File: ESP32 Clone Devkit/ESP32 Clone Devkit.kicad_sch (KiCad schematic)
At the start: 34 parts, among them J1 USB_B_Micro, J2 Conn_01x19_Pin, J3 Conn_01x19_Pin, Q1 MMSS8050-H-TP, Q2 MMSS8050-H-TP, SW1 SW_Push, SW2 SW_Push, U1 CP2102N-A02-GQFN28, U2 AMS1117-3.3

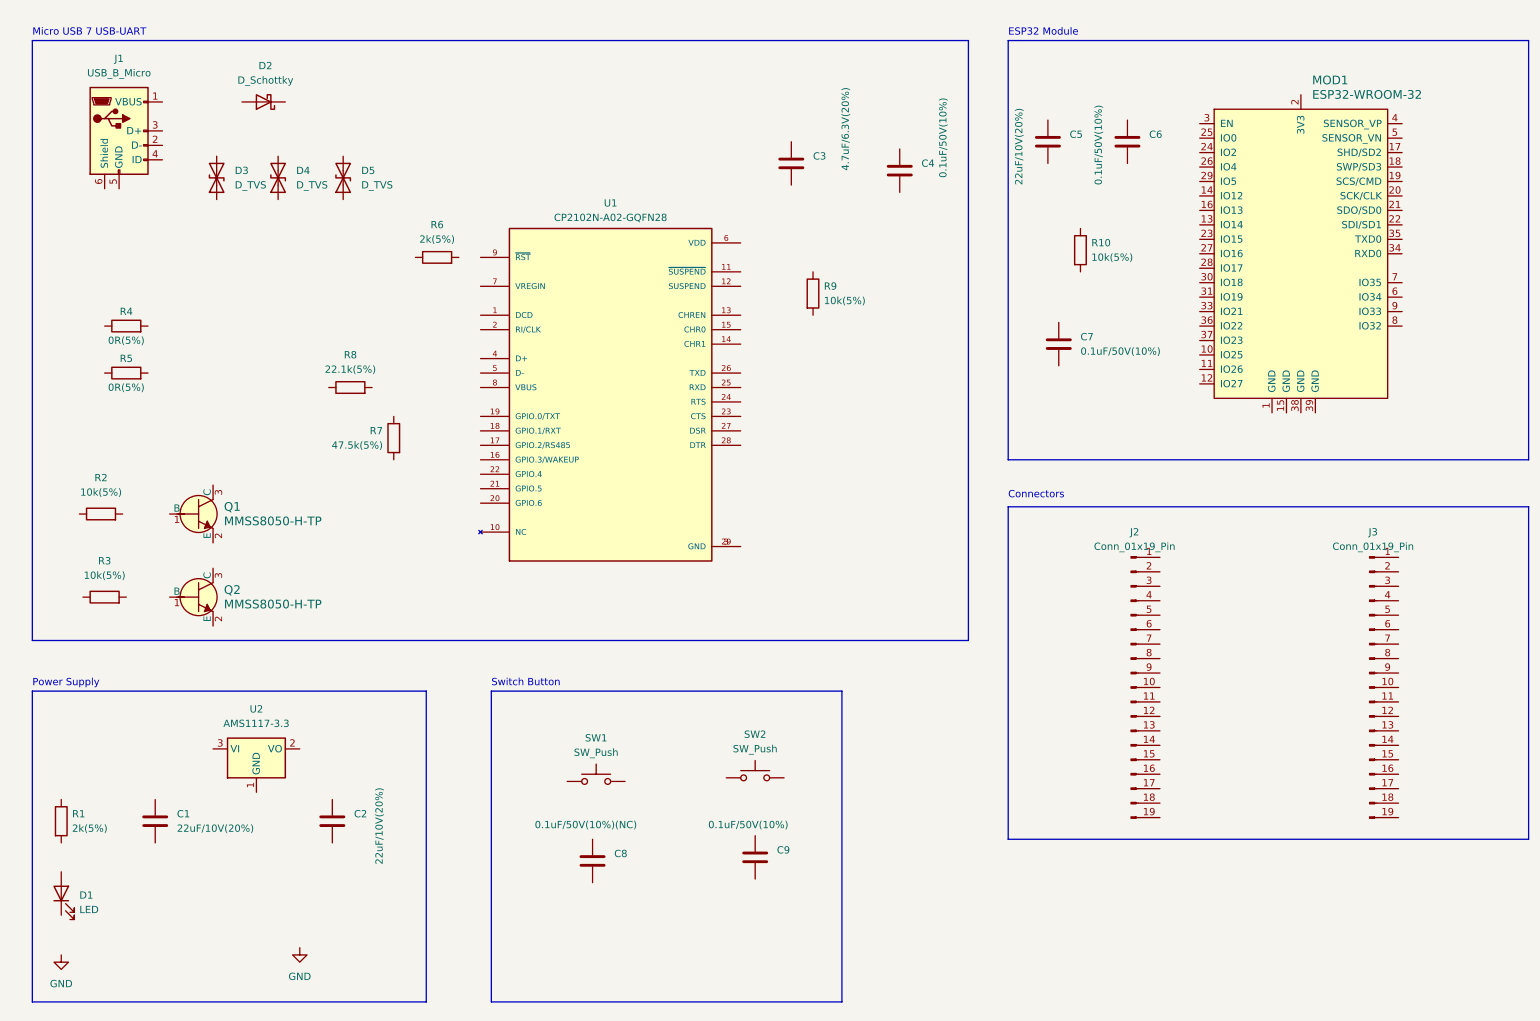
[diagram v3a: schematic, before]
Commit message: terminate wiring
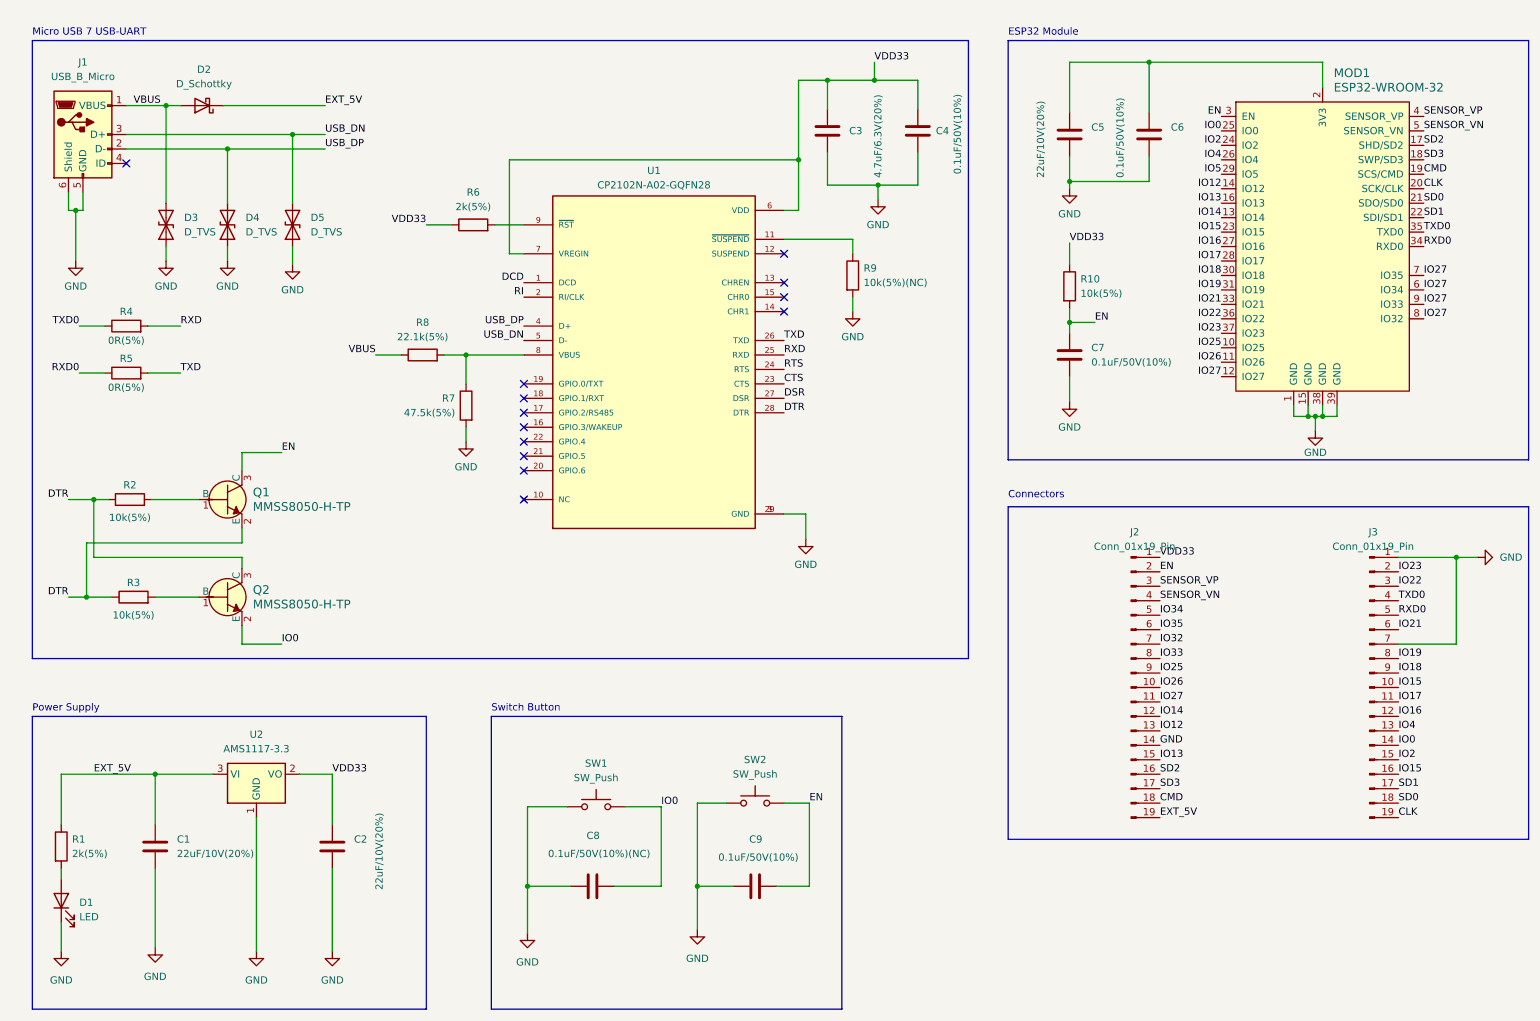
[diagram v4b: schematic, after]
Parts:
- R9: value 10k(5%) -> 10k(5%)(NC)
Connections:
- net GND: now also C1.2, C2.2, C3.2, C4.2, C5.2, C6.2, C7.2, C8.1, C9.1, D1.1 (K), D3.1 (A1), D4.1 (A1), D5.1 (A1), J1.5 (GND), J1.6 (Shield), J2.14 (Pin_14), J3.1 (Pin_1), J3.7 (Pin_7), MOD1.1 (GND), MOD1.15 (GND), MOD1.38 (GND), MOD1.39 (GND), R7.2, R9.2, SW1.1, SW2.1, U1.29 (GND), U1.3 (GND), U2.1 (GND)
- net VDD33: now reaches C3.1
- net VDD33: now also C2.1, C4.1, J2.1 (Pin_1), R10.1, R6.1, U1.6 (VDD), U1.7 (VREGIN), U2.2 (VO)
- net at Q2.1 (B): now also R3.2
- net IO0: now reaches Q2.2 (E)
- net IO0: now also C8.2, J3.14 (Pin_14), MOD1.25 (IO0), SW1.2
- net DTR: now reaches Q2.3 (C)
- net DTR: now also Q1.2 (E), R2.1, R3.1, U1.28 (DTR)
- net EXT_5V: now reaches R1.1
- net EXT_5V: now also C1.1, D2.1 (K), J2.19 (Pin_19), U2.3 (VI)
- net at R1.2: now also D1.2 (A)
- net at R6.2: now also U1.9 (~{RST})
- net at Q1.1 (B): now also R2.2
- net EN: now reaches Q1.3 (C)
- net EN: now also C7.1, C9.2, J2.2 (Pin_2), MOD1.3 (EN), R10.2, SW2.2
- net USB_DN: now reaches D5.2 (A2)
- net USB_DN: now also J1.3 (D+), U1.5 (D-)
- net at R7.1: now also R8.2, U1.8 (VBUS)
- net IO15: now reaches J3.10 (Pin_10)
- net IO15: now also J3.16 (Pin_16), MOD1.23 (IO15)
- net IO17: now reaches J3.11 (Pin_11)
- net IO17: now also MOD1.28 (IO17)
- net IO16: now reaches J3.12 (Pin_12)
- net IO16: now also MOD1.27 (IO16)
- net IO4: now reaches J3.13 (Pin_13)
- net IO4: now also MOD1.26 (IO4)
- net IO2: now reaches J3.15 (Pin_15)
- net IO2: now also MOD1.24 (IO2)
- net SD1: now reaches J3.17 (Pin_17)
- net SD1: now also MOD1.22 (SDI/SD1)
- net SD0: now reaches J3.18 (Pin_18)
- net SD0: now also MOD1.21 (SDO/SD0)
- net CLK: now reaches J3.19 (Pin_19)
- net CLK: now also MOD1.20 (SCK/CLK)
- net IO23: now reaches J3.2 (Pin_2)
- net IO23: now also MOD1.37 (IO23)
- net IO22: now reaches J3.3 (Pin_3)
- net IO22: now also MOD1.36 (IO22)
- net TXD0: now reaches J3.4 (Pin_4)
- net TXD0: now also MOD1.35 (TXD0), R4.1
- net RXD0: now reaches J3.5 (Pin_5)
- net RXD0: now also MOD1.34 (RXD0), R5.1
- net IO21: now reaches J3.6 (Pin_6)
- net IO21: now also MOD1.33 (IO21)
- net IO19: now reaches J3.8 (Pin_8)
- net IO19: now also MOD1.31 (IO19)
- net IO18: now reaches J3.9 (Pin_9)
- net IO18: now also MOD1.30 (IO18)
- net DCD: now reaches U1.1 (DCD)
- net at U1.11 (~{SUSPEND}): now also R9.1
- net RI: now reaches U1.2 (RI/CLK)
- net CTS: now reaches U1.23 (CTS)
- net RTS: now reaches U1.24 (RTS)
- net RXD: now reaches U1.25 (RXD)
- net RXD: now also R4.2
- net TXD: now reaches U1.26 (TXD)
- net TXD: now also R5.2
- net DSR: now reaches U1.27 (DSR)
- net USB_DP: now reaches U1.4 (D+)
- net USB_DP: now also D4.2 (A2), J1.2 (D-)
- net IO26: now reaches J2.10 (Pin_10)
- net IO26: now also MOD1.11 (IO26)
- net IO27: now reaches J2.11 (Pin_11)
- net IO27: now also MOD1.12 (IO27), MOD1.6 (IO34), MOD1.7 (IO35), MOD1.8 (IO32), MOD1.9 (IO33)
- net IO14: now reaches J2.12 (Pin_12)
- net IO14: now also MOD1.13 (IO14)
- net IO12: now reaches J2.13 (Pin_13)
- net IO12: now also MOD1.14 (IO12)
- net IO13: now reaches J2.15 (Pin_15)
- net IO13: now also MOD1.16 (IO13)
- net SD2: now reaches J2.16 (Pin_16)
- net SD2: now also MOD1.17 (SHD/SD2)
- net SD3: now reaches J2.17 (Pin_17)
- net SD3: now also MOD1.18 (SWP/SD3)
- net CMD: now reaches J2.18 (Pin_18)
- net CMD: now also MOD1.19 (SCS/CMD)
- net SENSOR_VP: now reaches J2.3 (Pin_3)
- net SENSOR_VP: now also MOD1.4 (SENSOR_VP)
- net SENSOR_VN: now reaches J2.4 (Pin_4)
- net SENSOR_VN: now also MOD1.5 (SENSOR_VN)
- net IO34: now reaches J2.5 (Pin_5)
- net IO35: now reaches J2.6 (Pin_6)
- net IO32: now reaches J2.7 (Pin_7)
- net IO33: now reaches J2.8 (Pin_8)
- net IO25: now reaches J2.9 (Pin_9)
- net IO25: now also MOD1.10 (IO25)
- net VBUS: now reaches D3.2 (A2)
- net VBUS: now also D2.2 (A), J1.1 (VBUS), R8.1
- net at MOD1.2 (3V3): now also C5.1, C6.1
- net IO5: now reaches MOD1.29 (IO5)
- no-connect marks 0 -> 13
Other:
- moved on the sheet: C1, C2, C3, C4, C5, C6, C7, C8, C9, D1, D2, D3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

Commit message: add nets Classes
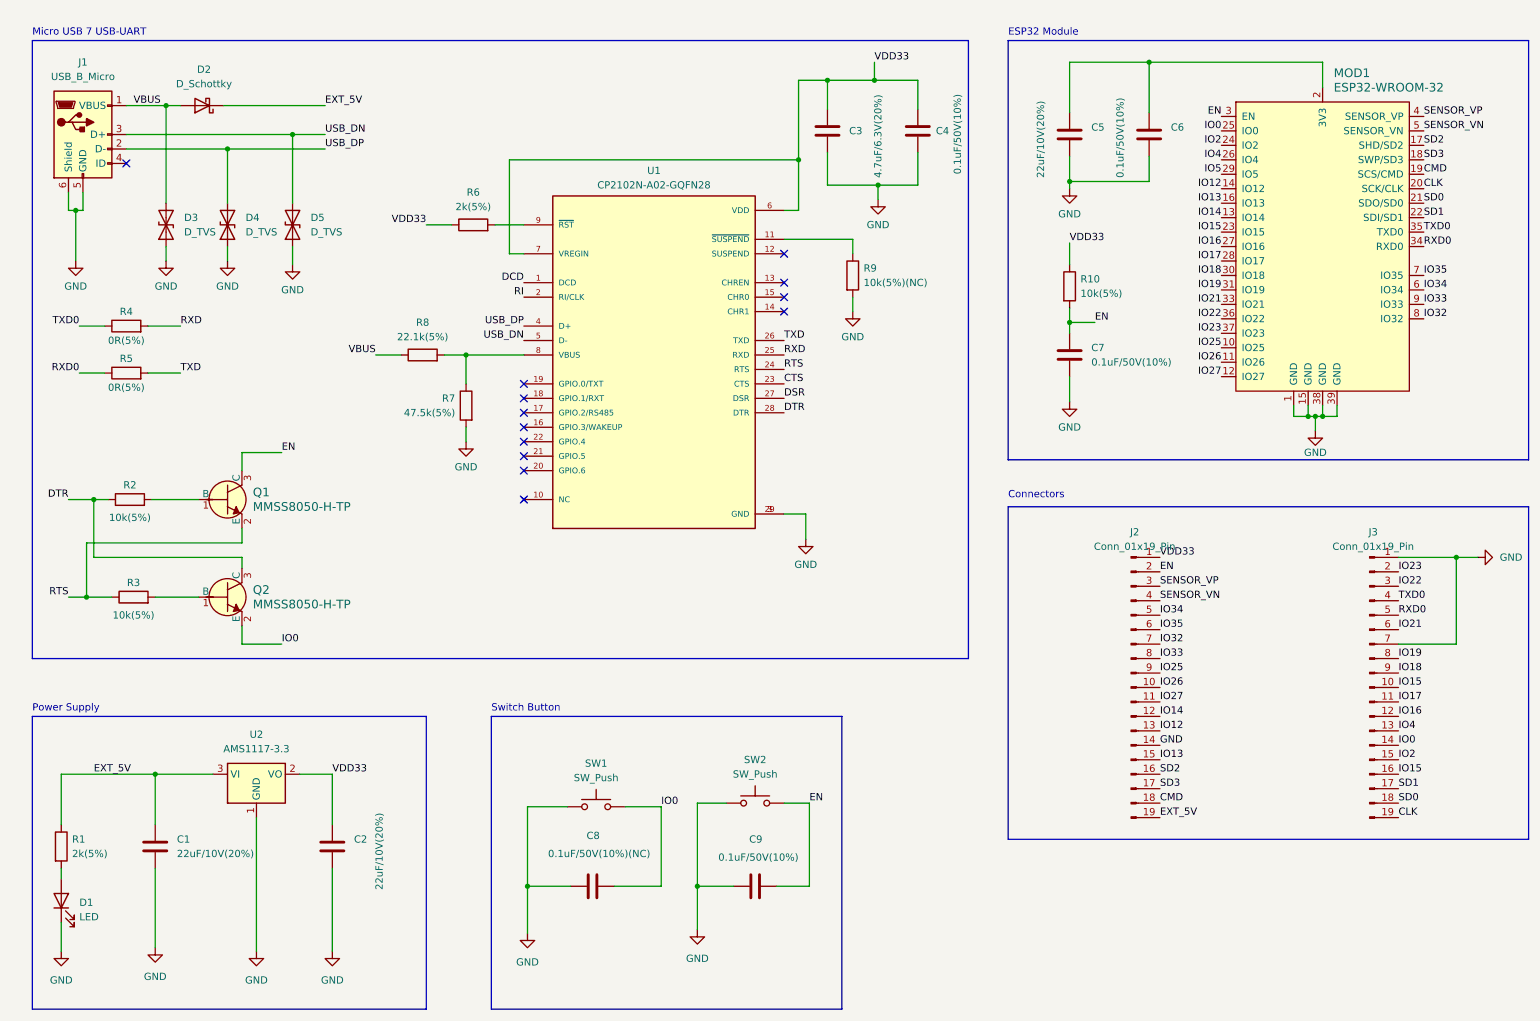
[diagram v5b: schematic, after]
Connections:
- net DTR: no longer Q1.2 (E), R3.1
- net IO27: no longer MOD1.6 (IO34), MOD1.7 (IO35), MOD1.8 (IO32), MOD1.9 (IO33)
- net IO32: now also MOD1.8 (IO32)
- net IO33: now also MOD1.9 (IO33)
- net IO34: now also MOD1.6 (IO34)
- net IO35: now also MOD1.7 (IO35)
- net RTS: now also Q1.2 (E), R3.1
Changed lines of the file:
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@@
     (effects (font (size 1.27 1.27)) (justify left bottom))
   )
-  (label "IO27" (at 262.255 72.39 0) (fields_autoplaced)
+  (label "IO32" (at 262.255 72.39 0) (fields_autoplaced)
     (effects (font (size 1.27 1.27)) (justify left bottom))
   )
@@
     (effects (font (size 1.27 1.27)) (justify right bottom))
   )
-  (label "DTR" (at 24.13 121.285 180) (fields_autoplaced)
+  (label "RTS" (at 24.13 121.285 180) (fields_autoplaced)
     (effects (font (size 1.27 1.27)) (justify right bottom))
   )
@@
     (effects (font (size 1.27 1.27)) (justify left bottom))
   )
-  (label "IO27" (at 262.255 69.85 0) (fields_autoplaced)
+  (label "IO33" (at 262.255 69.85 0) (fields_autoplaced)
     (effects (font (size 1.27 1.27)) (justify left bottom))
   )
@@
     (effects (font (size 1.27 1.27)) (justify left bottom))
   )
-  (label "IO27" (at 262.255 67.31 0) (fields_autoplaced)
+  (label "IO34" (at 262.255 67.31 0) (fields_autoplaced)
     (effects (font (size 1.27 1.27)) (justify left bottom))
   )
@@
     (effects (font (size 1.27 1.27)) (justify right bottom))
   )
-  (label "IO27" (at 262.255 64.77 0) (fields_autoplaced)
-    (effects (font (size 1.27 1.27)) (justify left bottom))
-  )
+  (label "IO35" (at 262.255 64.77 0) (fields_autoplaced)
+    (effects (font (size 1.27 1.27)) (justify left bottom))
+  )

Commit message: add comments
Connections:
- net IO15: no longer J3.10 (Pin_10)
- net IO5: now also J3.10 (Pin_10)
- no-connect marks 13 -> 12
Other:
- note added: "Auto programm DTR RTS --> EN IO0 1 1 1 1 0 0 1 1 1 0 0 1 0 1 1 0"
- moved on the sheet: R7, R8
